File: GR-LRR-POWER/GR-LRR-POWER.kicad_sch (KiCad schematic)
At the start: 50 parts, among them J1 DT13-08PB, J2 DT13-08PB, J3 Switch, J4 Switch, J5 Switch, U1 SIS434DN-T1-GE3, U2 SIS434DN-T1-GE3, U3 LTC4365CTS8-TRMPBF, U4 696108003002, U5 696108003002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

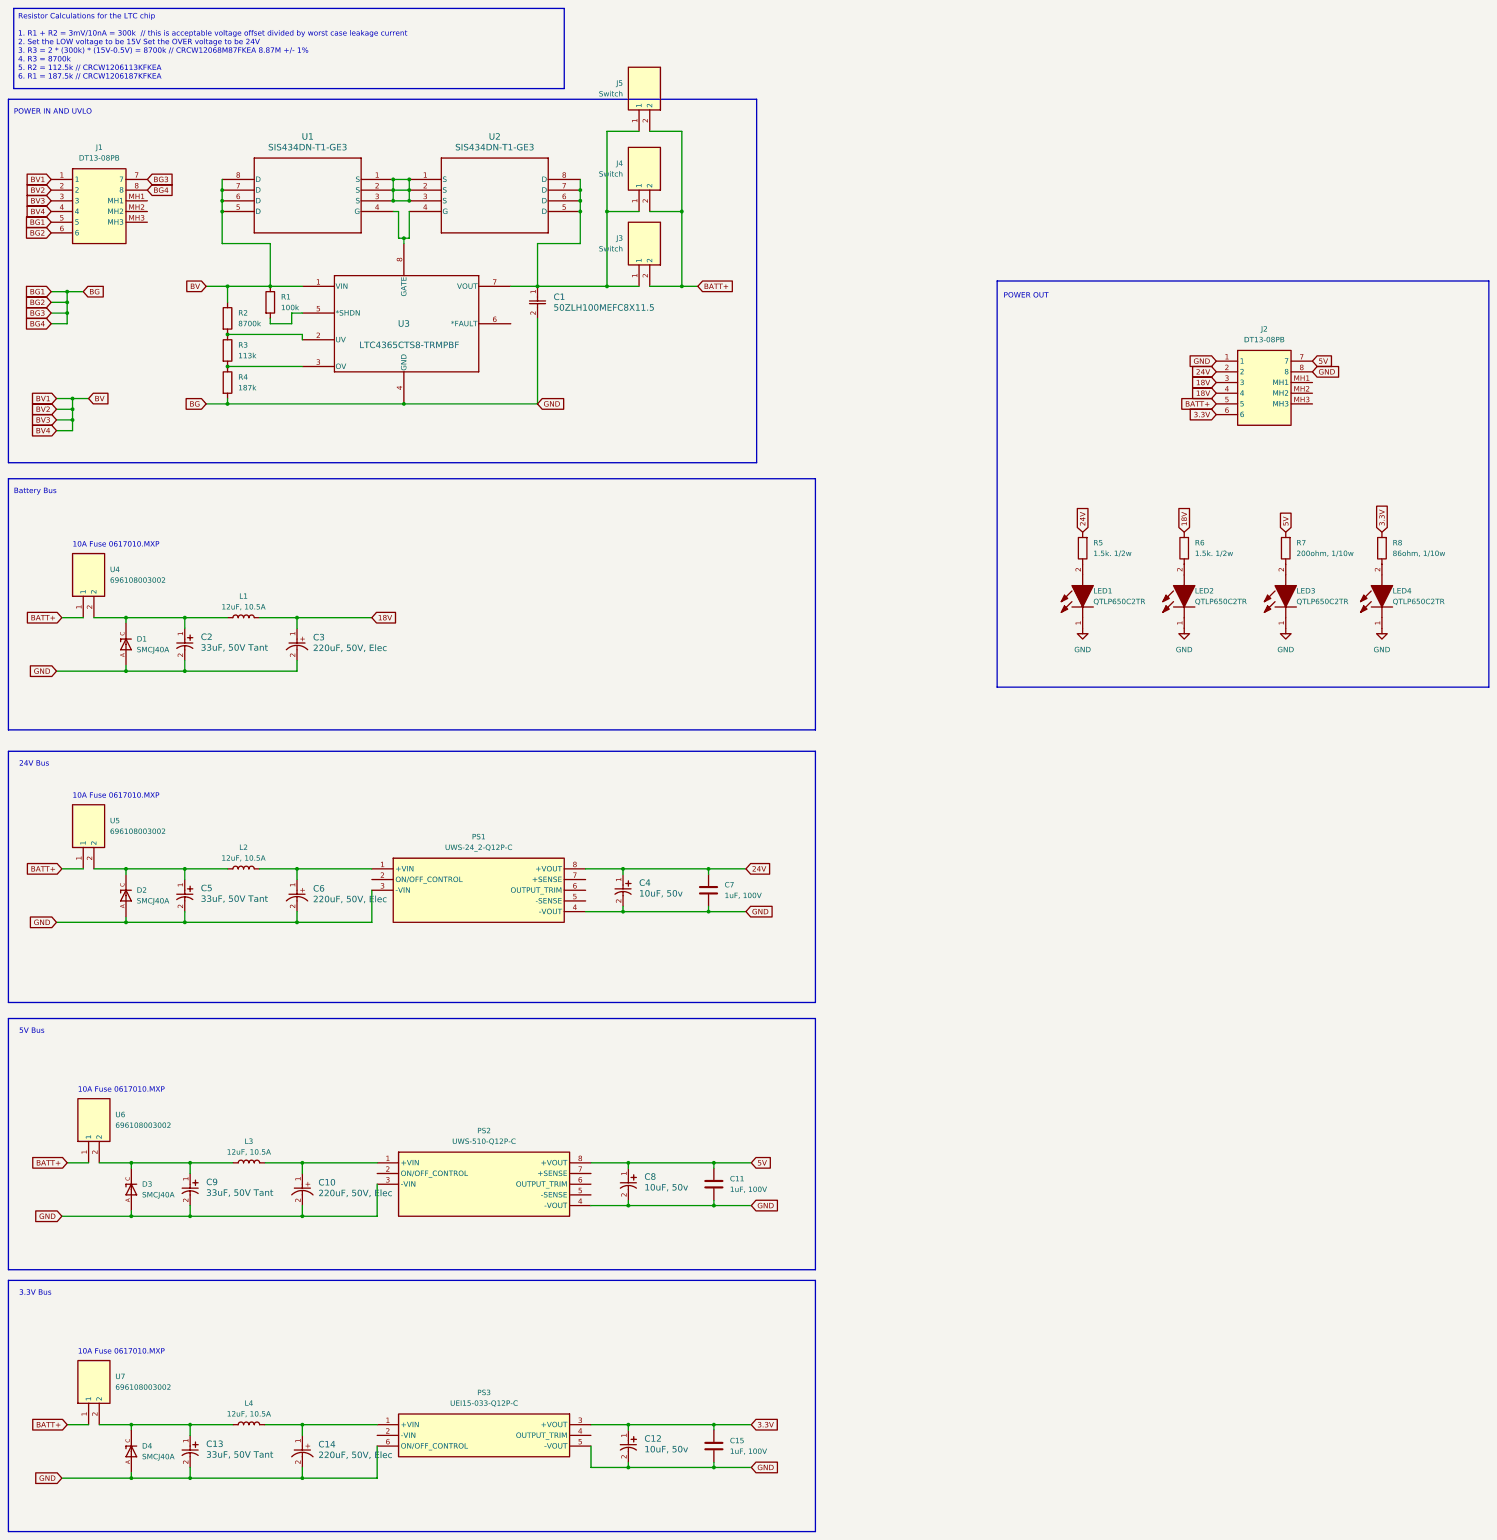
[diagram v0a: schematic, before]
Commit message: purchasing A3 power
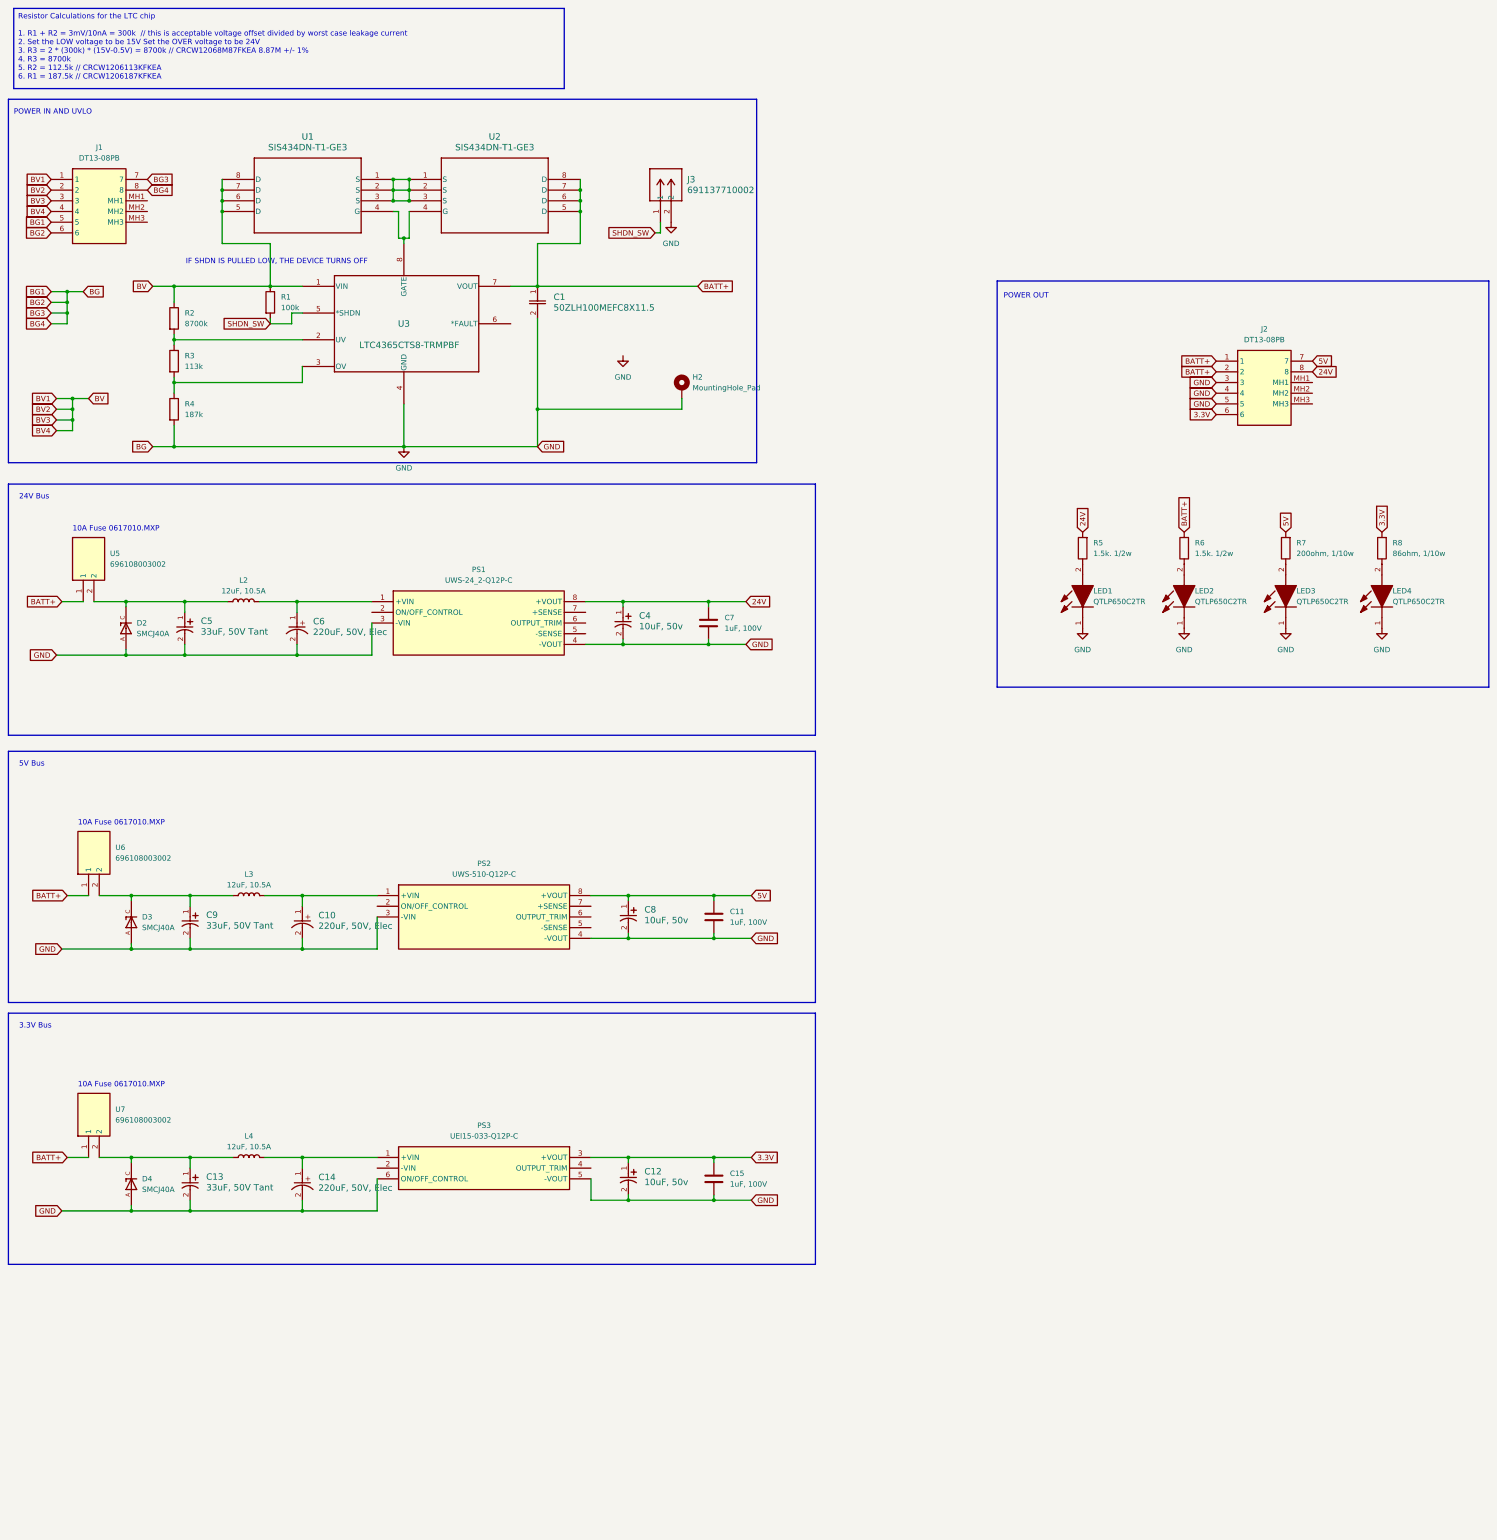
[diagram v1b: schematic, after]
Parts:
- removed C2: 33uF, 50V Tant, avid_footprints:CAPMP7.6X4.3_4.3N_KEM-L, symbol T521X336M050ATE075:T521X336M050ATE075
- removed C3: 220uF, 50V, Elec, avid_footprints:U2-R_NCH-L, symbol UWT1H221MNL1GS:UWT1H221MNL1GS
- removed D1: SMCJ40A, avid_footprints:DIOM7959X262N, symbol SMCJ40A:SMCJ40A
- removed J3, J4, J5: Switch, 212520-1002, symbol 212520-1002:212520-1002
- removed L1: 12uF, 10.5A, Inductor_SMD:L_Coilcraft_XAL8080-XXX, symbol Device:L
- removed U4: 696108003002, avid_footprints:WR-FSH_THT_2, symbol 696108003002:696108003002
- added H2: MountingHole_Pad, MountingHole:MountingHole_3mm_Pad_Via, symbol Mechanical:MountingHole_Pad
- added J3: 691137710002, avid_footprints:691137710002, symbol avid_symbols:691137710002
- U3: footprint TSOT-23_TS8_LIT -> avid_footprints:TSOT-23_TS8_LIT
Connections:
- net 24V: now also J2.8; no longer J2.2
- net BATT+: now also C1.1, J2.1, J2.2, R6.2, U2.5 (D), U2.6 (D), U2.7 (D), U2.8 (D), U3.7 (VOUT); no longer J2.5
- net GND: now also J2.3, J2.4, J2.5, H2.1, J3.2; no longer J2.1, J2.8
- net SHDN_SW: now reaches R1.2, U3.5 (*SHDN)
- net SHDN_SW: now also J3.1
- removed net 18V: J2.3, J2.4, R6.2
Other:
- note added: "IF SHDN IS PULLED LOW, THE DEVICE TURNS OFF"
- note removed: "Battery Bus"
- moved on the sheet: C10, C11, C12, C13, C14, C15, C4, C5, C6, C7, C8, C9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

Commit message: ordered power and control A4
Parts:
- added R10, R11, R9: 168, Resistor_SMD:R_1206_3216Metric_Pad1.30x1.75mm_HandSolder, symbol Device:R
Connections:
- net GND: now also R11.2
- net at PS3.4 (OUTPUT_TRIM): now also R11.1
- net at PS1.6 (OUTPUT_TRIM): now also R10.1
- net at PS1.7 (+SENSE): now also R10.2
- net at PS2.6 (OUTPUT_TRIM): now also R9.1
- net at PS2.7 (+SENSE): now also R9.2
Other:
- moved on the sheet: C11, C12, C15, C4, C7, C8

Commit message: upload
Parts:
- C1: Part Number (none) -> 50ZLH100MEFC8X11.5
- C10, C14, C6: Part Number (none) -> UWT1H221MNL1GS
- C13, C5, C9: Part Number T521X336M050ATE075 -> T521X336M050ATE050
- J1: Part Number (none) -> DT13-08PB
- J3: Part Number (none) -> 691137710002
- PS1: Part Number (none) -> UWS-24_2-Q12P-C
- PS2: Part Number (none) -> UWS-510-Q12P-C
- U1, U2: Part Number (none) -> SIS434DN-T1-GE3
- U3: Part Number (none) -> LTC4365CTS8-TRMPBF
- U5: Part Number (none) -> 696108003002
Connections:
- net GND: now also PS3.2 (-VIN); no longer PS3.6 (ON/OFF_CONTROL)
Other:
- note added: "-VIN was not connected"
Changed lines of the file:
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@@
 	(wire
 		(pts
-			(xy 109.22 299.72) (xy 109.22 307.34)
+			(xy 91.44 307.34) (xy 91.44 304.8)
 		)
 		(stroke
@@
 	(wire
 		(pts
-			(xy 91.44 307.34) (xy 91.44 304.8)
+			(xy 113.03 62.23) (xy 116.84 62.23)
 		)
 		(stroke
@@
 	(wire
 		(pts
-			(xy 113.03 62.23) (xy 116.84 62.23)
+			(xy 177.8 233.68) (xy 177.8 232.41)
 		)
 		(stroke
@@
 	(wire
 		(pts
-			(xy 177.8 233.68) (xy 177.8 232.41)
+			(xy 50.8 243.84) (xy 50.8 245.11)
 		)
 		(stroke
@@
 	(wire
 		(pts
-			(xy 50.8 243.84) (xy 50.8 245.11)
+			(xy 50.8 295.91) (xy 50.8 294.64)
 		)
 		(stroke
@@
 	(wire
 		(pts
-			(xy 50.8 295.91) (xy 50.8 294.64)
+			(xy 83.82 96.52) (xy 88.9 96.52)
 		)
 		(stroke
@@
 	(wire
 		(pts
-			(xy 83.82 96.52) (xy 88.9 96.52)
+			(xy 105.41 307.34) (xy 91.44 307.34)
 		)
 		(stroke
@@
 	(wire
 		(pts
-			(xy 109.22 307.34) (xy 91.44 307.34)
-		)
-		(stroke
-			(width 0)
-			(type default)
-		)
-	)
-	(wire
-		(pts
 			(xy 176.53 172.72) (xy 195.58 172.72)
 		)
@@
 	(wire
 		(pts
+			(xy 109.22 297.18) (xy 105.41 297.18)
+		)
+		(stroke
+			(width 0)
+			(type default)
+		)
+	)
+	(wire
+		(pts
 			(xy 41.91 162.56) (xy 49.53 162.56)
 		)
@@
 	(wire
 		(pts
+			(xy 105.41 297.18) (xy 105.41 307.34)
+		)
+		(stroke
+			(width 0)
+			(type default)
+		)
+	)
+	(wire
+		(pts
 			(xy 91.44 232.41) (xy 91.44 234.95)
 		)
@@
 		)
 	)
+	(text "-VIN was not connected"
+		(exclude_from_sim no)
+		(at 100.584 285.496 0)
+		(effects
+			(font
+				(size 1.27 1.27)
+			)
+		)
+	)
 	(text "IF SHDN IS PULLED LOW, THE DEVICE TURNS OFF\n"
 		(exclude_from_sim no)
@@
 			)
 		)
+		(property "Part Number" "SIS434DN-T1-GE3"
+			(at 113.03 62.23 0)
+			(effects
+				(font
+					(size 1.27 1.27)
+				)
+				(hide yes)
+			)
+		)
 		(pin "1"
 		)
@@
 			)
 		)
-		(property "Part Number" "T521X336M050ATE075"
+		(property "Part Number" "T521X336M050ATE050"
 			(at 64.77 297.18 90)
 			(effects
@@
 			)
 		)
+		(property "Part Number" "SIS434DN-T1-GE3"
+			(at 116.84 62.23 0)
+			(effects
+				(font
+					(size 1.27 1.27)
+				)
+				(hide yes)
+			)
+		)
 		(pin "1"
 		)
@@
 			)
 		)
+		(property "Part Number" "UWT1H221MNL1GS"
+			(at 91.44 297.18 90)
+			(effects
+				(font
+					(size 1.27 1.27)
+				)
+				(hide yes)
+			)
+		)
 		(pin "1"
 		)
@@
 			)
 		)
+		(property "Part Number" "UWT1H221MNL1GS"
+			(at 91.44 234.95 90)
+			(effects
+				(font
+					(size 1.27 1.27)
+				)
+				(hide yes)
+			)
+		)
+		(property "Field6" ""
+			(at 91.44 234.95 90)
+			(effects
+				(font
+					(size 1.27 1.27)
+				)
+				(hide yes)
+			)
+		)
 		(pin "1"
 		)
@@
 			)
 		)
+		(property "Part Number" "UWS-24_2-Q12P-C"
+			(at 107.95 162.56 0)
+			(effects
+				(font
+					(size 1.27 1.27)
+				)
+				(hide yes)
+			)
+		)
 		(pin "1"
 		)
@@
 			)
 		)
-		(property "Part Number" "T521X336M050ATE075"
+		(property "Part Number" "T521X336M050ATE050"
 			(at 63.5 165.1 90)
 			(effects
@@
 			)
 		)
-		(property "Part Number" "T521X336M050ATE075"
+		(property "Part Number" "T521X336M050ATE050"
 			(at 64.77 234.95 90)
 			(effects
@@
 			)
 		)
+		(property "Part Number" "LTC4365CTS8-TRMPBF"
+			(at 115.57 96.52 0)
+			(effects
+				(font
+					(size 1.27 1.27)
+				)
+				(hide yes)
+			)
+		)
 		(pin "1"
 		)
@@
 			)
 		)
+		(property "Part Number" "691137710002"
+			(at 176.53 72.39 90)
+			(effects
+				(font
+					(size 1.27 1.27)
+				)
+				(hide yes)
+			)
+		)
 		(pin "1"
 		)
@@
 			)
 		)
+		(property "Part Number" "696108003002"
+			(at 39.37 162.56 90)
+			(effects
+				(font
+					(size 1.27 1.27)
+				)
+				(hide yes)
+			)
+		)
 		(pin "1"
 		)
@@
 			)
 		)
+		(property "Part Number" "50ZLH100MEFC8X11.5"
+			(at 147.32 87.63 90)
+			(effects
+				(font
+					(size 1.27 1.27)
+				)
+				(hide yes)
+			)
+		)
 		(pin "1"
 		)
@@
 			)
 		)
+		(property "Part Number" "UWS-510-Q12P-C"
+			(at 109.22 232.41 0)
+			(effects
+				(font
+					(size 1.27 1.27)
+				)
+				(hide yes)
+			)
+		)
 		(pin "1"
 		)
@@
 			)
 		)
+		(property "Part Number" "UWT1H221MNL1GS"
+			(at 90.17 165.1 90)
+			(effects
+				(font
+					(size 1.27 1.27)
+				)
+				(hide yes)
+			)
+		)
 		(pin "1"
 		)
@@
 				(hide yes)
 			)
+		)
+		(property "Part Number" "DT13-08PB"
+			(at 31.75 62.23 0)
+			(effects
+				(font
+					(size 1.27 1.27)
+				)
+				(hide yes)
+			)
